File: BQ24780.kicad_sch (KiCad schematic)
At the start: 39 parts, among them Q2 BSS138, Q3 RBFET, Q4 HIGH, Q5 LOW, Q6 ACFET, U2 BQ24780SRUYR

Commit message: Working on contours
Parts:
- C10, C11, C12, C13, C3, C4, C5: footprint Resistor_SMD:R_0603_1608Metric -> Capacitor_SMD:C_0603_1608Metric
- C14, C15, C7, C8: footprint Capacitor_SMD:C_1206_3216Metric -> Capacitor_SMD:C_0603_1608Metric
- Q3, Q4, Q5, Q6: footprint libs:CSD18543Q3A -> footprints:CSD18543Q3A
- U2: footprint libs:BQ24780SRUYR -> footprints:BQ24780SRUYR
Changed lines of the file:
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@@
     )
   )
-  (symbol (lib_name "CSD18543Q3A_1") (lib_id "CSD18543Q3A:CSD18543Q3A") (at 48.26 35.56 90) (unit 1)
+  (symbol (lib_id "CSD18543Q3A:CSD18543Q3A") (at 48.26 35.56 90) (unit 1)
     (in_bom yes) (on_board yes) (dnp no)
     (property "Reference" "Q6" (at 48.26 26.67 90)
@@
       (effects (font (size 1.27 1.27)))
     )
-    (property "Footprint" "libs:CSD18543Q3A" (at 49.784 35.56 0)
+    (property "Footprint" "footprints:CSD18543Q3A" (at 49.784 35.56 0)
       (effects (font (size 1.524 1.524)) hide)
     )
@@
       (effects (font (size 1.27 1.27)))
     )
-    (property "Footprint" "libs:CSD18543Q3A" (at 216.535 94.234 0)
+    (property "Footprint" "footprints:CSD18543Q3A" (at 216.535 94.234 0)
       (effects (font (size 1.524 1.524)) hide)
     )
@@
       (effects (font (size 1.27 1.27)) (justify right))
     )
-    (property "Footprint" "Capacitor_SMD:C_1206_3216Metric" (at 259.08 106.68 0)
+    (property "Footprint" "Capacitor_SMD:C_0603_1608Metric" (at 259.08 106.68 0)
       (effects (font (size 1.27 1.27)) hide)
     )
@@
       (effects (font (size 1.27 1.27)) (justify right))
     )
-    (property "Footprint" "Resistor_SMD:R_0603_1608Metric" (at 96.52 48.26 0)
+    (property "Footprint" "Capacitor_SMD:C_0603_1608Metric" (at 96.52 48.26 0)
       (effects (font (size 1.27 1.27)) hide)
     )
@@
       (effects (font (size 1.27 1.27)) (justify right))
     )
-    (property "Footprint" "Capacitor_SMD:C_1206_3216Metric" (at 133.35 39.37 0)
+    (property "Footprint" "Capacitor_SMD:C_0603_1608Metric" (at 133.35 39.37 0)
       (effects (font (size 1.27 1.27)) hide)
     )
@@
       (effects (font (size 1.27 1.27)) (justify right))
     )
-    (property "Footprint" "Resistor_SMD:R_0603_1608Metric" (at 106.68 48.26 0)
+    (property "Footprint" "Capacitor_SMD:C_0603_1608Metric" (at 106.68 48.26 0)
       (effects (font (size 1.27 1.27)) hide)
     )
@@
       (effects (font (size 1.27 1.27)))
     )
-    (property "Footprint" "Resistor_SMD:R_0603_1608Metric" (at 101.6 41.91 0)
+    (property "Footprint" "Capacitor_SMD:C_0603_1608Metric" (at 101.6 41.91 0)
       (effects (font (size 1.27 1.27)) hide)
     )
@@
       (effects (font (size 1.27 1.27)) (justify right))
     )
-    (property "Footprint" "Resistor_SMD:R_0603_1608Metric" (at 237.49 114.935 0)
+    (property "Footprint" "Capacitor_SMD:C_0603_1608Metric" (at 237.49 114.935 0)
       (effects (font (size 1.27 1.27)) hide)
     )
@@
       (effects (font (size 1.27 1.27)))
     )
-    (property "Footprint" "libs:CSD18543Q3A" (at 77.851 35.56 0)
+    (property "Footprint" "footprints:CSD18543Q3A" (at 77.851 35.56 0)
       (effects (font (size 1.524 1.524)) hide)
     )
@@
       (effects (font (size 1.524 1.524)))
     )
-    (property "Footprint" "libs:BQ24780SRUYR" (at 156.21 117.094 0)
+    (property "Footprint" "footprints:BQ24780SRUYR" (at 156.21 117.094 0)
       (effects (font (size 1.524 1.524)) hide)
     )
-    (property "Datasheet" "" (at 156.21 115.57 0)
-      (effects (font (size 1.524 1.524)))
+    (property "Datasheet" "https://www.ti.com/lit/gpn/bq24780s" (at 156.21 115.57 0)
+      (effects (font (size 1.524 1.524)) hide)
     )
     (pin "1")
@@
       (effects (font (size 1.27 1.27)) (justify right))
     )
-    (property "Footprint" "Capacitor_SMD:C_1206_3216Metric" (at 270.51 106.68 0)
+    (property "Footprint" "Capacitor_SMD:C_0603_1608Metric" (at 270.51 106.68 0)
       (effects (font (size 1.27 1.27)) hide)
     )
@@
       (effects (font (size 1.27 1.27)) (justify right))
     )
-    (property "Footprint" "Resistor_SMD:R_0603_1608Metric" (at 247.65 114.935 0)
+    (property "Footprint" "Capacitor_SMD:C_0603_1608Metric" (at 247.65 114.935 0)
       (effects (font (size 1.27 1.27)) hide)
     )
@@
       (effects (font (size 1.27 1.27)) (justify right))
     )
-    (property "Footprint" "Capacitor_SMD:C_1206_3216Metric" (at 144.78 39.37 0)
+    (property "Footprint" "Capacitor_SMD:C_0603_1608Metric" (at 144.78 39.37 0)
       (effects (font (size 1.27 1.27)) hide)
     )
@@
       (effects (font (size 1.27 1.27)) (justify right))
     )
-    (property "Footprint" "Resistor_SMD:R_0603_1608Metric" (at 205.105 114.935 0)
+    (property "Footprint" "Capacitor_SMD:C_0603_1608Metric" (at 205.105 114.935 0)
       (effects (font (size 1.27 1.27)) hide)
     )
@@
       (effects (font (size 1.27 1.27)))
     )
-    (property "Footprint" "Resistor_SMD:R_0603_1608Metric" (at 242.57 108.585 0)
+    (property "Footprint" "Capacitor_SMD:C_0603_1608Metric" (at 242.57 108.585 0)
       (effects (font (size 1.27 1.27)) hide)
     )
@@
       (effects (font (size 1.27 1.27)))
     )
-    (property "Footprint" "libs:CSD18543Q3A" (at 216.535 112.014 0)
+    (property "Footprint" "footprints:CSD18543Q3A" (at 216.535 112.014 0)
       (effects (font (size 1.524 1.524)) hide)
     )

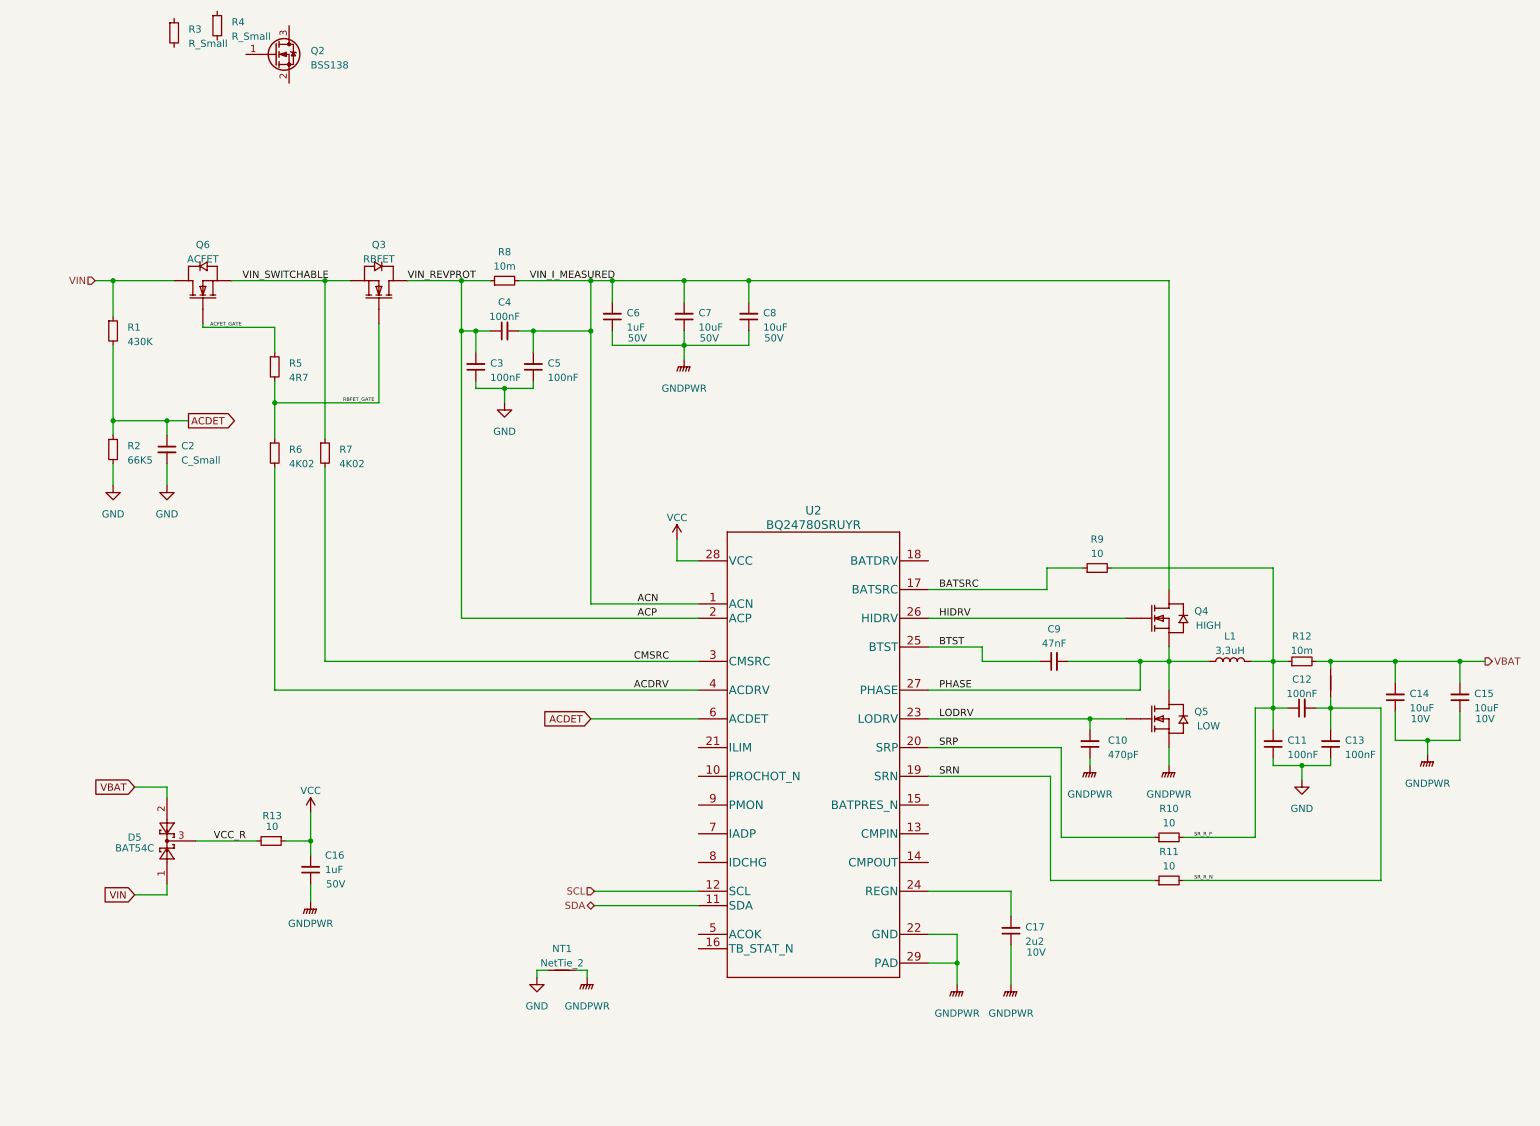
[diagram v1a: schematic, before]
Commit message: Added gate protection circuit to the SCH
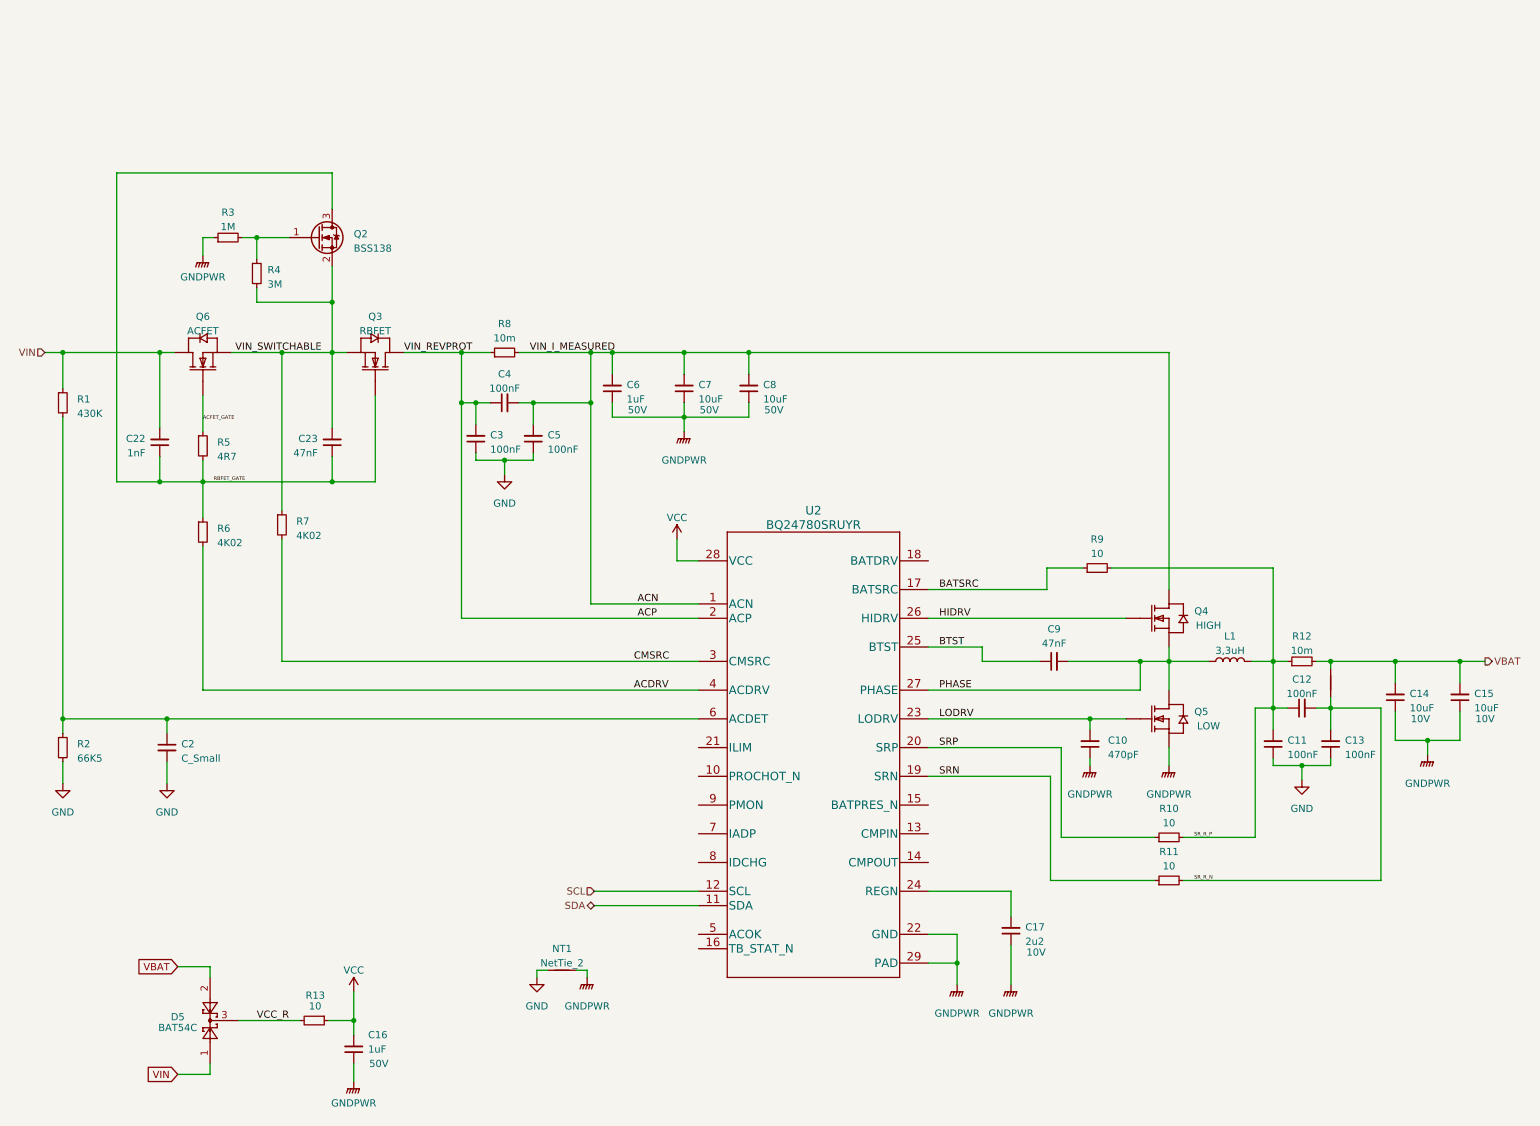
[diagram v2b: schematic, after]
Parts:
- added C22: 1nF, Capacitor_SMD:C_0603_1608Metric, symbol Device:C_Small
- added C23: 47nF, Capacitor_SMD:C_0603_1608Metric, symbol Device:C_Small
- R3: value R_Small -> 1M
- R4: value R_Small -> 3M
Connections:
- net GNDPWR: now also R3.1
- net RBFET_GATE: now also Q2.3 (D), C22.1, C23.1
- net VIN: now also C22.2
- net VIN_SWITCHABLE: now also Q2.2 (S), R4.2, C23.2
- net at R4.1: now also Q2.1 (G), R3.2
- net ACDET: no longer names the net of C2.1, R1.2, R2.1, U2.6 (ACDET)
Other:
- moved on the sheet: C16, C2, C3, C4, C5, C6, C7, C8, D5, Q2, Q3, Q6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

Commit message: ERC pass
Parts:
- added R26, R27: TBD, Resistor_SMD:R_0603_1608Metric, symbol Device:R_Small
- added R28: 10K, Resistor_SMD:R_0603_1608Metric, symbol Device:R_Small
- Q3, Q4, Q5, Q6: footprint footprints:CSD18543Q3A -> DNH0008A
- U2: footprint footprints:BQ24780SRUYR -> RUY0028A
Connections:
- net GND: now also U2.13 (CMPIN), U2.15 (BATPRES_N), R26.2
- net at U2.10 (PROCHOT_N): now also R28.2
- net TB_STAT: now reaches U2.16 (TB_STAT_N)
- net ILIM: now reaches U2.21 (ILIM)
- net ILIM: now also R26.1, R27.2
- net ACOK: now reaches U2.5 (ACOK)
- net ACN renamed VIN_I_MEASURED
- net ACP renamed VIN_REVPROT
- new net +3V3: R27.1, R28.1
- no-connect marks 0 -> 5
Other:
- moved on the sheet: C10, C11, C12, C13, C17, C22, C23, C9, NT1, Q4, Q5, R1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

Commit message: Board routed
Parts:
- C2: value C_Small -> 100nF; footprint (none) -> Capacitor_SMD:C_0603_1608Metric; Voltage (none) -> 25V
- L1: footprint libs:IND_ETQP5M150YFK -> Inductor_SMD:L_Bourns-SRN8040_8x8.15mm; PN (none) -> IHLP3232DZER3R3M01
- Q3, Q4, Q5, Q6: footprint DNH0008A -> footprints:CSD18543Q3A
- U2: footprint RUY0028A -> footprints:BQ24780SRUYR
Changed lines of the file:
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@@
+    (stroke (width 0) (type default))
+  )
+  (wire (pts (xy 95.25 120.65) (xy 135.89 120.65))
     (stroke (width 0) (type default))
   )
@@
   )
   (wire (pts (xy 259.08 100.33) (xy 270.51 100.33))
-    (stroke (width 0) (type default))
-  )
-  (wire (pts (xy 95.25 120.65) (xy 135.89 120.65))
     (stroke (width 0) (type default))
   )
@@
       (effects (font (size 1.27 1.27)))
     )
-    (property "Footprint" "DNH0008A" (at 49.784 48.26 0)
+    (property "Footprint" "footprints:CSD18543Q3A" (at 49.784 48.26 0)
       (effects (font (size 1.524 1.524)) hide)
     )
@@
   )
   (symbol (lib_id "Device:C_Small") (at 41.91 115.57 0) (unit 1)
-    (in_bom yes) (on_board yes) (dnp no) (fields_autoplaced)
+    (in_bom yes) (on_board yes) (dnp no)
     (property "Reference" "C2" (at 44.45 114.9413 0)
       (effects (font (size 1.27 1.27)) (justify left))
     )
-    (property "Value" "C_Small" (at 44.45 117.4813 0)
+    (property "Value" "100nF" (at 44.45 117.4813 0)
       (effects (font (size 1.27 1.27)) (justify left))
     )
-    (property "Footprint" "" (at 41.91 115.57 0)
+    (property "Footprint" "Capacitor_SMD:C_0603_1608Metric" (at 41.91 115.57 0)
       (effects (font (size 1.27 1.27)) hide)
     )
@@
       (effects (font (size 1.27 1.27)) hide)
     )
+    (property "Voltage" "25V" (at 44.45 119.38 0)
+      (effects (font (size 1.27 1.27)) (justify left))
+    )
     (pin "1")
     (pin "2")
@@
       (effects (font (size 1.27 1.27)))
     )
-    (property "Footprint" "DNH0008A" (at 217.17 94.234 0)
+    (property "Footprint" "footprints:CSD18543Q3A" (at 217.17 94.234 0)
       (effects (font (size 1.524 1.524)) hide)
     )
@@
       (effects (font (size 1.27 1.27)))
     )
-    (property "Footprint" "libs:IND_ETQP5M150YFK" (at 229.87 100.33 0)
-      (effects (font (size 1.27 1.27)) hide)
-    )
-    (property "Datasheet" "~" (at 229.87 100.33 0)
+    (property "Footprint" "Inductor_SMD:L_Bourns-SRN8040_8x8.15mm" (at 229.87 100.33 0)
+      (effects (font (size 1.27 1.27)) hide)
+    )
+    (property "Datasheet" "https://hu.mouser.com/datasheet/2/427/ihlp_3232dz_01-1763002.pdf" (at 229.87 100.33 0)
+      (effects (font (size 1.27 1.27)) hide)
+    )
+    (property "PN" "IHLP3232DZER3R3M01" (at 229.87 100.33 90)
       (effects (font (size 1.27 1.27)) hide)
     )
@@
       (effects (font (size 1.27 1.27)))
     )
-    (property "Footprint" "DNH0008A" (at 77.216 48.26 0)
+    (property "Footprint" "footprints:CSD18543Q3A" (at 77.216 48.26 0)
       (effects (font (size 1.524 1.524)) hide)
     )
@@
       (effects (font (size 1.524 1.524)))
     )
-    (property "Footprint" "RUY0028A" (at 156.21 117.094 0)
+    (property "Footprint" "footprints:BQ24780SRUYR" (at 156.21 117.094 0)
       (effects (font (size 1.524 1.524)) hide)
     )
@@
       (effects (font (size 1.27 1.27)))
     )
-    (property "Footprint" "DNH0008A" (at 217.17 112.014 0)
+    (property "Footprint" "footprints:CSD18543Q3A" (at 217.17 112.014 0)
       (effects (font (size 1.524 1.524)) hide)
     )
